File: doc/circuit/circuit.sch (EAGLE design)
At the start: 19 parts, among them U1 LPC1114FN28/102

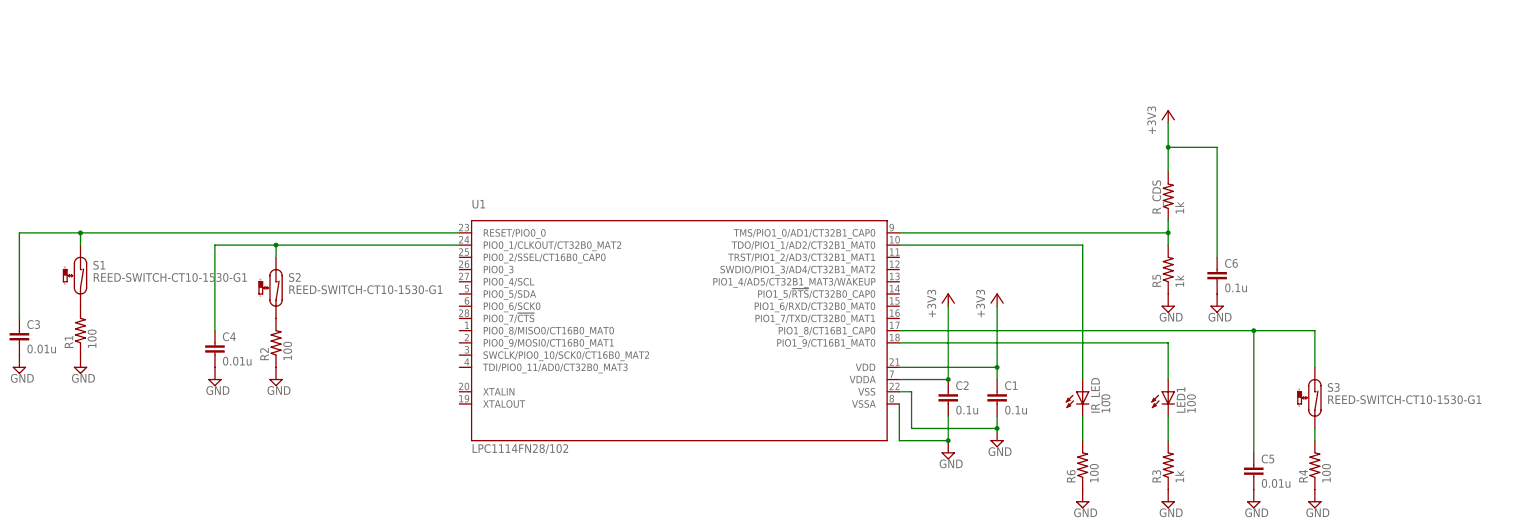
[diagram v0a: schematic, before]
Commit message: fixes #210.
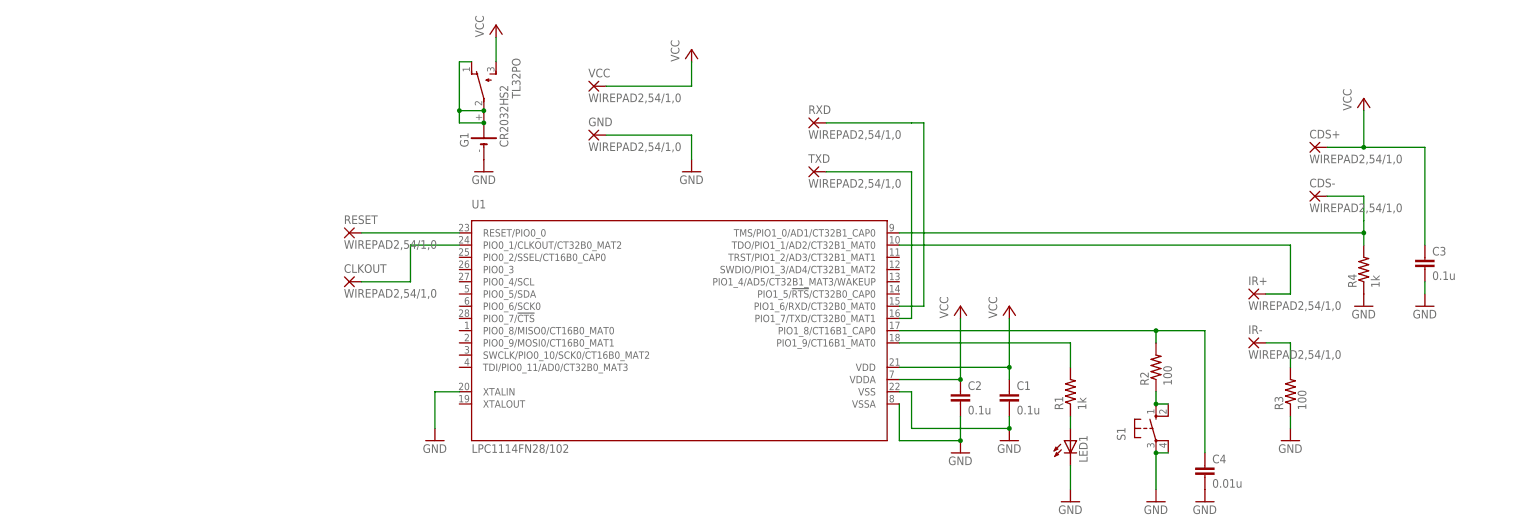
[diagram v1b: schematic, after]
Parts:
- removed C5: 0.01u, rcl:C-EU050-024X044
- removed C6: 0.1u, rcl:C-EU050-024X044
- removed IR_LED: 100, led:LED5MM
- removed R5, R_CDS: 1k, rcl:R-US_0204/7
- removed R6: 100, rcl:R-US_0204/7
- removed S3: REED-SWITCH-CT10-1530-G1, switch-reed:REED-SWITCH-CT10-1530-G1
- added CDS+, CDS-, CLKOUT, GND, IR+, IR-, RESET, RXD, TXD, VCC: WIREPAD2,54/1,0, wirepad:WIREPAD2,54/1,0
- added G1: CR2032H, battery:CR2032H
- C1, C2, C4: device rcl:C-EU050-024X044 -> rcl:C-EU025-024X044
- C3: value 0.01u -> 0.1u; device rcl:C-EU050-024X044 -> rcl:C-EU025-024X044
- LED1: value 100 -> (none)
- R1, R4: value 100 -> 1k
- R3: value 1k -> 100
- S1: value REED-SWITCH-CT10-1530-G1 -> (none); device switch-reed:REED-SWITCH-CT10-1530-G1 -> switch-omron:10-XX
- S2: value REED-SWITCH-CT10-1530-G1 -> TL32PO; device switch-reed:REED-SWITCH-CT10-1530-G1 -> switch:TL32PO
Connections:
- removed net +3V3: C1.1, C2.1, C6.1, R_CDS.2, U1.VDD, U1.VDDA
- removed net N$10: LED1.C, R3.2
- removed net N$11: IR_LED.C, R6.2
- new net GND2: TXD.P, U1.PIO1_7/TXD/CT32B0_MAT1
- new net VCC: C1.1, C2.1, C3.1, CDS+.P, S2.S, U1.VDD, U1.VDDA, VCC.P
- new net VCC1: IR+.P, U1.TDO/PIO1_1/AD2/CT32B1_MAT0
- new net VCC3: RXD.P, U1.PIO1_6/RXD/CT32B0_MAT0
- net GND: now also G1.-, GND.P, LED1.C, S1.P, S1.P1, U1.XTALIN; no longer C5.2, C6.2, R1.1, R2.1, R5.1, R6.1
- net N$1: now also IR-.P, R3.2; no longer R1.2, S1.2
- net N$2: now also R2.1, S1.S, S1.S1; no longer C3.1, S1.1, U1.RESET/PIO0_0
- net N$3: now also RESET.P, U1.RESET/PIO0_0; no longer R2.2, S2.2
- net N$4: now also CLKOUT.P; no longer C4.1, S2.1
- net N$5: now also G1.+, G1.+@1, S2.O, S2.P; no longer IR_LED.A, U1.TDO/PIO1_1/AD2/CT32B1_MAT0
- net N$6: now also R1.2; no longer LED1.A
- net N$7: now also C4.1, R2.2; no longer C5.1, S3.1
- net N$8: now also LED1.A, R1.1; no longer R4.2, S3.2
- net N$9: now also CDS-.P, R4.2; no longer R5.2, R_CDS.1
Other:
- moved on the sheet: C1, C2, C3, C4, LED1, R1, R2, R3, R4

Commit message: Added docs.
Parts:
- CDS+, CDS-, CLKOUT, GND, IR+, IR-, RESET, RXD, TXD, VCC: value WIREPAD2,54/1,0 -> WIREPAD2,15/1,0; device wirepad:WIREPAD2,54/1,0 -> wirepad:WIREPAD2,15/1,0
- R2: value 100 -> 1k
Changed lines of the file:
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@@
 <part name="LED1" library="led" deviceset="LED" device="5MM"/>
 <part name="R1" library="rcl" deviceset="R-US_" device="0204/7" value="1k"/>
-<part name="R2" library="rcl" deviceset="R-US_" device="0204/7" value="100"/>
+<part name="R2" library="rcl" deviceset="R-US_" device="0204/7" value="1k"/>
 <part name="C4" library="rcl" deviceset="C-EU" device="025-024X044" value="0.01u"/>
 <part name="R4" library="rcl" deviceset="R-US_" device="0204/7" value="1k"/>
@@
 <part name="GND1" library="supply1" deviceset="GND" device=""/>
 <part name="P+1" library="supply1" deviceset="VCC" device=""/>
-<part name="VCC" library="wirepad" deviceset="WIREPAD" device="2,54/1,0"/>
+<part name="VCC" library="wirepad" deviceset="WIREPAD" device="2,15/1,0" value="WIREPAD2,15/1,0"/>
 <part name="GND2" library="supply1" deviceset="GND" device=""/>
 <part name="GND3" library="supply1" deviceset="GND" device=""/>
@@
 <part name="GND5" library="supply1" deviceset="GND" device=""/>
 <part name="P+4" library="supply1" deviceset="VCC" device=""/>
-<part name="CDS+" library="wirepad" deviceset="WIREPAD" device="2,54/1,0"/>
-<part name="CDS-" library="wirepad" deviceset="WIREPAD" device="2,54/1,0"/>
+<part name="CDS+" library="wirepad" deviceset="WIREPAD" device="2,15/1,0" value="WIREPAD2,15/1,0"/>
+<part name="CDS-" library="wirepad" deviceset="WIREPAD" device="2,15/1,0" value="WIREPAD2,15/1,0"/>
 <part name="GND6" library="supply1" deviceset="GND" device=""/>
 <part name="GND7" library="supply1" deviceset="GND" device=""/>
 <part name="GND8" library="supply1" deviceset="GND" device=""/>
-<part name="IR+" library="wirepad" deviceset="WIREPAD" device="2,54/1,0"/>
-<part name="IR-" library="wirepad" deviceset="WIREPAD" device="2,54/1,0"/>
+<part name="IR+" library="wirepad" deviceset="WIREPAD" device="2,15/1,0" value="WIREPAD2,15/1,0"/>
+<part name="IR-" library="wirepad" deviceset="WIREPAD" device="2,15/1,0" value="WIREPAD2,15/1,0"/>
 <part name="GND9" library="supply1" deviceset="GND" device=""/>
 <part name="S1" library="switch-omron" deviceset="10-XX" device=""/>
-<part name="GND" library="wirepad" deviceset="WIREPAD" device="2,54/1,0"/>
-<part name="RESET" library="wirepad" deviceset="WIREPAD" device="2,54/1,0"/>
-<part name="CLKOUT" library="wirepad" deviceset="WIREPAD" device="2,54/1,0"/>
+<part name="GND" library="wirepad" deviceset="WIREPAD" device="2,15/1,0" value="WIREPAD2,15/1,0"/>
+<part name="RESET" library="wirepad" deviceset="WIREPAD" device="2,15/1,0" value="WIREPAD2,15/1,0"/>
+<part name="CLKOUT" library="wirepad" deviceset="WIREPAD" device="2,15/1,0" value="WIREPAD2,15/1,0"/>
 <part name="GND10" library="supply1" deviceset="GND" device=""/>
-<part name="RXD" library="wirepad" deviceset="WIREPAD" device="2,54/1,0"/>
-<part name="TXD" library="wirepad" deviceset="WIREPAD" device="2,54/1,0"/>
+<part name="RXD" library="wirepad" deviceset="WIREPAD" device="2,15/1,0" value="WIREPAD2,15/1,0"/>
+<part name="TXD" library="wirepad" deviceset="WIREPAD" device="2,15/1,0" value="WIREPAD2,15/1,0"/>
 <part name="G1" library="battery" deviceset="CR2032H" device=""/>
 <part name="GND11" library="supply1" deviceset="GND" device=""/>
